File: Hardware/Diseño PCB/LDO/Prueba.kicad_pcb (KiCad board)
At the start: 2 copper layers, 100 x 100 mm, 61 parts, among them Q1 2N3904, Q10 BC557, Q11 BC547, Q12 BC557, Q13 BC557, Q14 BC547, Q15 BC557, Q16 BC547, Q17 BC557, Q18 BC547, Q19 BC547, Q2 BC547, Q3 BC547, Q4 BC557, Q5 BC557, Q6 BC547, Q7 BC547, Q8 IRF4905, Q9 BC547, U1 TL431LP, U4 LM324

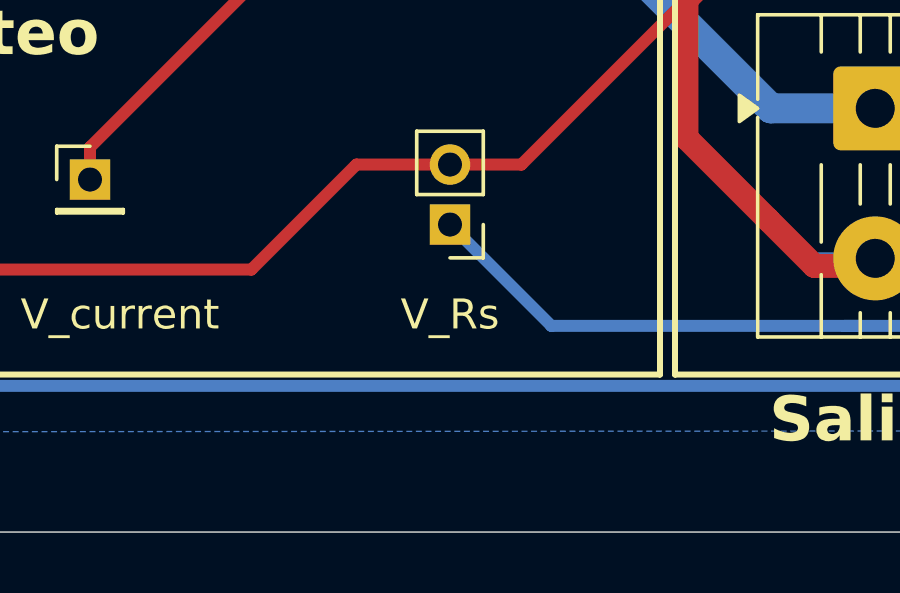
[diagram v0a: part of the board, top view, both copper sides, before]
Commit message: CHK3 : Creación de latex para CHK3 individual
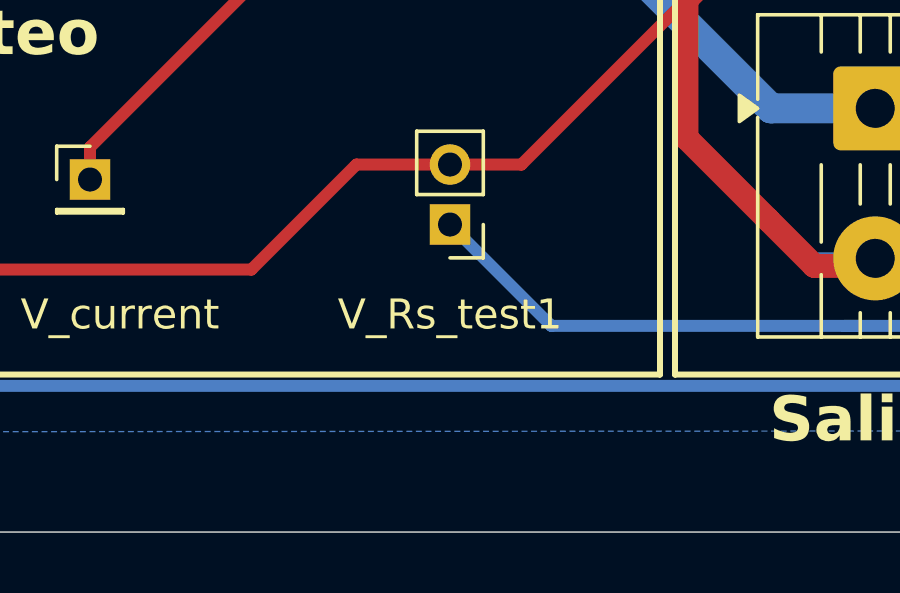
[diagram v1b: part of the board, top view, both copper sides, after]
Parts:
- Q13, Q15, Q17, Q4, Q5: value BC557 -> 2N3906
- Q14, Q16, Q18, Q19, Q2, Q3, Q6, Q7: value BC547 -> 2N3904
- renumbered V_Rs to V_Rs_test1
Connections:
- R1 pad 2: Net-(Q1-B) -> Net-(Q20-B)
- U1 pad 3: Net-(Q1-B) -> Net-(Q20-B)
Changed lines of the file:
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@@
 			)
 		)
-		(property "Value" "BC557"
+		(property "Value" "2N3906"
 			(at 1.27 2.79 0)
 			(layer "F.Fab")
@@
 			)
 		)
-		(property "Value" "BC547"
+		(property "Value" "2N3904"
 			(at 1.27 2.79 0)
 			(layer "F.Fab")
@@
 			(layers "*.Cu" "*.Mask")
 			(remove_unused_layers no)
-			(net "Net-(Q1-B)")
+			(net "Net-(Q20-B)")
 			(pinfunction "K_3")
 			(pintype "passive")
@@
 			)
 		)
-		(property "Value" "BC547"
+		(property "Value" "2N3904"
 			(at 1.27 2.79 90)
 			(layer "F.Fab")
@@
 			)
 		)
-		(property "Value" "BC547"
+		(property "Value" "2N3904"
 			(at 1.27 2.79 90)
 			(layer "F.Fab")
@@
 			)
 		)
-		(property "Value" "BC557"
+		(property "Value" "2N3906"
 			(at 1.27 2.79 90)
 			(layer "F.Fab")
@@
 			)
 		)
-		(property "Value" "BC547"
+		(property "Value" "2N3904"
 			(at 1.27 2.79 0)
 			(layer "F.Fab")
@@
 			(layers "*.Cu" "*.Mask")
 			(remove_unused_layers no)
-			(net "Net-(Q1-B)")
+			(net "Net-(Q20-B)")
 			(pintype "passive")
 		)
@@
 			)
 		)
-		(property "Value" "BC547"
+		(property "Value" "2N3904"
 			(at 1.27 2.79 90)
 			(layer "F.Fab")
@@
 			)
 		)
-		(property "Value" "BC547"
+		(property "Value" "2N3904"
 			(at 1.27 2.79 0)
 			(layer "F.Fab")
@@
 			)
 		)
-		(property "Value" "BC557"
+		(property "Value" "2N3906"
 			(at 1.27 2.79 90)
 			(layer "F.Fab")
@@
 			)
 		)
-		(property "Value" "BC547"
+		(property "Value" "2N3904"
 			(at 1.27 2.79 0)
 			(layer "F.Fab")
@@
 			)
 		)
-		(property "Value" "BC547"
+		(property "Value" "2N3904"
 			(at 1.27 2.79 90)
 			(layer "F.Fab")
@@
 		(descr "Through hole straight pin header, 1x02, 2.00mm pitch, single row")
 		(tags "Through hole pin header THT 1x02 2.00mm single row")
-		(property "Reference" "V_Rs"
+		(property "Reference" "V_Rs_test1"
 			(at 0 -3 0)
 			(layer "F.SilkS")
@@
 			)
 		)
-		(property "Value" "BC557"
+		(property "Value" "2N3906"
 			(at 1.27 2.79 90)
 			(layer "F.Fab")
@@
 			)
 		)
-		(property "Value" "BC557"
+		(property "Value" "2N3906"
 			(at 1.27 2.79 90)
 			(layer "F.Fab")

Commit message: CHK3: Agregue emergency version , pistas y esquematico al informe
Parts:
- removed G***: LOGO, LOGO
- removed Q1, Q14, Q16, Q18, Q19, Q7: 2N3904, Package_TO_SOT_THT:TO-92_Inline
- removed Q13, Q15, Q17: 2N3906, Package_TO_SOT_THT:TO-92_Inline
- removed U1: TL431LP, Package_TO_SOT_THT:TO-92_Inline
- removed U4: LM324, Package_DIP:DIP-14_W10.16mm_LongPads
- removed V_current: V_current_test, Connector_PinHeader_2.00mm:PinHeader_1x01_P2.00mm_Vertical
- removed V_ref_c: V_ref_c_test, Connector_PinHeader_2.00mm:PinHeader_1x01_P2.00mm_Vertical
- removed V_ref_t: V_ref_test, Connector_PinHeader_2.00mm:PinHeader_1x01_P2.00mm_Vertical
- removed V_voltage: V_voltage_test, Connector_PinHeader_2.00mm:PinHeader_1x01_P2.00mm_Vertical
- added Jc1: JC, Connector_PinHeader_2.00mm:PinHeader_1x03_P2.00mm_Vertical, F.Cu at (66.0, 165.0)
- added Jv2: JV, Connector_PinHeader_2.00mm:PinHeader_1x03_P2.00mm_Vertical, F.Cu at (66.0, 147.5)
- added LM324: LM324, Package_DIP:DIP-14_W10.16mm_LongPads, F.Cu at (87.3, 189.3)
- added Q20: BC547, Package_TO_SOT_THT:TO-92_HandSolder, F.Cu at (178.5, 43.3)
- added Q21: BC547, Package_TO_SOT_THT:TO-92_HandSolder, F.Cu at (167.8, 43.3)
- added Q22: BC547, Package_TO_SOT_THT:TO-92_HandSolder, F.Cu at (151.0, 53.5)
- added Q23: BC547, Package_TO_SOT_THT:TO-92_HandSolder, F.Cu at (158.5, 51.0)
- added Q24: BC547, Package_TO_SOT_THT:TO-92_HandSolder, F.Cu at (50.2, 240.3)
- added Q25: BC547, Package_TO_SOT_THT:TO-92_HandSolder, F.Cu at (73.5, 252.0)
- added Q26: BC547, Package_TO_SOT_THT:TO-92_HandSolder, F.Cu at (80.5, 252.0)
- added Q27: BC547, Package_TO_SOT_THT:TO-92_HandSolder, F.Cu at (73.5, 261.0)
- added Q28: BC547, Package_TO_SOT_THT:TO-92_HandSolder, F.Cu at (108.6, 29.6)
- added TL431: TL431LP, Package_TO_SOT_THT:TO-92_HandSolder, F.Cu at (98.4, 43.4)
- added V_ctrl1: V_Ctrl, Connector_PinHeader_2.00mm:PinHeader_1x01_P2.00mm_Vertical, F.Cu at (108.9, 224.5)
- added V_current_ref_test1: V_current_ref_test, Connector_PinHeader_2.00mm:PinHeader_1x01_P2.00mm_Vertical, F.Cu at (95.0, 224.5)
- added V_ref_c_test1: V_ref_c_test1, Connector_PinHeader_2.00mm:PinHeader_1x01_P2.00mm_Vertical, F.Cu at (113.0, 224.5)
- added V_ref_t_test1: V_ref_t_test, Connector_PinHeader_2.00mm:PinHeader_1x01_P2.00mm_Vertical, F.Cu at (99.1, 224.5)
- added V_voltage_test1: V_voltage_test, Connector_PinHeader_2.00mm:PinHeader_1x01_P2.00mm_Vertical, F.Cu at (117.0, 224.5)
- Q10, Q11, Q12, Q9: footprint Package_TO_SOT_THT:TO-92_Inline -> Package_TO_SOT_THT:TO-92_HandSolder
- Q2, Q3, Q6: value 2N3904 -> BC557; footprint Package_TO_SOT_THT:TO-92_Inline -> Package_TO_SOT_THT:TO-92_HandSolder
- Q4, Q5: value 2N3906 -> BC557; footprint Package_TO_SOT_THT:TO-92_Inline -> Package_TO_SOT_THT:TO-92_HandSolder
- RV1, RV2: footprint Potentiometer_THT:Potentiometer_Bourns_3266W_Vertical -> Potentiometer_THT:Potentiometer_Bourns_3339P_Vertical_HandSoldering
- moved R4 142.2 mm to (149.2, 36.5), turned to 0 degrees
- moved Q2 139.0 mm to (178.5, 33.8)
- moved Q3 136.0 mm to (167.8, 33.8), turned to 90 degrees
- moved RV1 135.8 mm to (135.5, 36.3), turned to 0 degrees
- moved R3 135.4 mm to (149.2, 31.0)
- moved R13 134.6 mm to (149.2, 42.0), turned to 0 degrees
- moved Q4 133.5 mm to (21.2, 248.5), turned to 0 degrees
- moved R6 131.7 mm to (120.4, 29.8)
- moved Q5 130.0 mm to (37.2, 252.6), turned to 0 degrees
- moved R2 127.5 mm to (110.4, 44.7), turned to 90 degrees
- moved Q6 126.9 mm to (31.5, 264.0)
- moved R5 126.1 mm to (120.6, 38.1), turned to 0 degrees
- moved R1 120.9 mm to (98.4, 36.7), turned to 90 degrees
- moved Rs1 83.6 mm to (23.4, 209.3), turned to 0 degrees
- moved R7 83.2 mm to (23.4, 165.2)
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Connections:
- C_comp_t1 pad 1: GND -> Vref
- C_comp_t1 pad 2: Vref -> Net-(Q20-B)
- Q10 pad 2: V_current_ref -> Net-(Jc1-Pin_2)
- Q12 pad 2: V_voltage -> Net-(Jv2-Pin_2)
- Q2 pad 1: Net-(Q2-E) -> V_voltage
- Q2 pad 2: VF_fv -> Net-(Q2-B)
- Q2 pad 3: Net-(Q2-C) -> Vcc
- Q3 pad 1: Net-(Q2-E) -> Net-(Q2-B)
- Q3 pad 2: Net-(Q3-B) -> Net-(Q2-B)
- Q3 pad 3: V_voltage -> Vcc
- Q4 pad 1: Vcc -> V_current
- Q4 pad 2: Net-(Q2-C) -> Net-(Q25-C)
- Q4 pad 3: V_voltage -> Vcc
- Q5 pad 1: Vcc -> Net-(Q25-C)
- Q5 pad 2: Net-(Q2-C) -> Net-(Q25-C)
- Q5 pad 3: Net-(Q2-C) -> Vcc
- Q6 pad 1: GND -> Vctrl
- Q6 pad 2: nodo A -> Net-(Q27-C)
- Q6 pad 3: nodo A -> Vcc
- R13 pad 2: Net-(Q3-B) -> Net-(Q20-B)
- R3 pad 1: Net-(Q3-B) -> Net-(Q20-B)
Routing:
- net GND: track 351.2 -> 44.2 mm
- net Vref_c: track 255.7 -> 0.00 mm
- net Vcc: track 248.1 -> 26.5 mm
- net Vref: track 198.2 -> 40.0 mm
- net -V_Rs: track 162.4 -> 8.12 mm
- net V_voltage: track 133.9 -> 14.7 mm
- net VF_fv: track 130.7 -> 22.6 mm
- net +V_Rs: track 101.8 -> 0.00 mm
- net nodo A: track 71.7 -> 0.00 mm
- net V_current_ref: track 62.4 -> 0.00 mm
- net Vctrl: track 52.4 -> 0.00 mm
- net VF_fa: track 51.3 -> 0.00 mm
- net Net-(U4A-+): track 47.6 -> 0.00 mm
- net Net-(Q20-E): track 0.00 -> 38.2 mm
- net Net-(Q14-E): track 33.4 -> 0.00 mm
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- removed copper zone on B.Cu, net GND
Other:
- outline, holes or cut-outs redrawn
- board text added: "Ampl At"
- board text added: "Conmut."
- board text added: "Grupo 7 : Regulador de baja caida (LDO, Low drop regulator)"
- board text added: "Lazo Corriente"
- board text added: "Lazo tensión"
- board text added: "Limit. C"
- board text added: "Vref_c"
- board text removed: "Ampli. aC"
- board text removed: "Ampli. aT"
- board text removed: "Conmutador"
- board text removed: "Entrada"
- board text removed: "GND"
- board text removed: "Grupo 7: Regulador de baja caída (LDO,Low Dropout Regulator)"
- board text removed: "Lazo Tensión"
- board text removed: "Lazo regulador de Corriente"
- board text removed: "Limitador C"
- board text removed: "OPAMS"
- board text removed: "Salida"
- board text removed: "TA138 - Taller de Diseño de Circuitos Electrónicos"
- board text removed: "Tensiones de Testeo"
- board text removed: "Transistor de Paso"
- board text removed: "Vref_C"
